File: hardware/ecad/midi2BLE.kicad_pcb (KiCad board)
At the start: 2 copper layers, 100 x 30 mm, 50 parts, among them J1 USB_C_Receptacle, J2 Conn_01x02, J4 Conn_01x07, J6 Conn_01x04, SW1 SW_Push, SW2 SW_Push, SW3 SW_SPDT, U1 BQ24079RGTT, U2 TPS62162DSG, U3 TLV61047DDC, U4 ESP32-S3-WROOM-1, U5 TPS2116DRL, U6 TS3USB30EDGSR

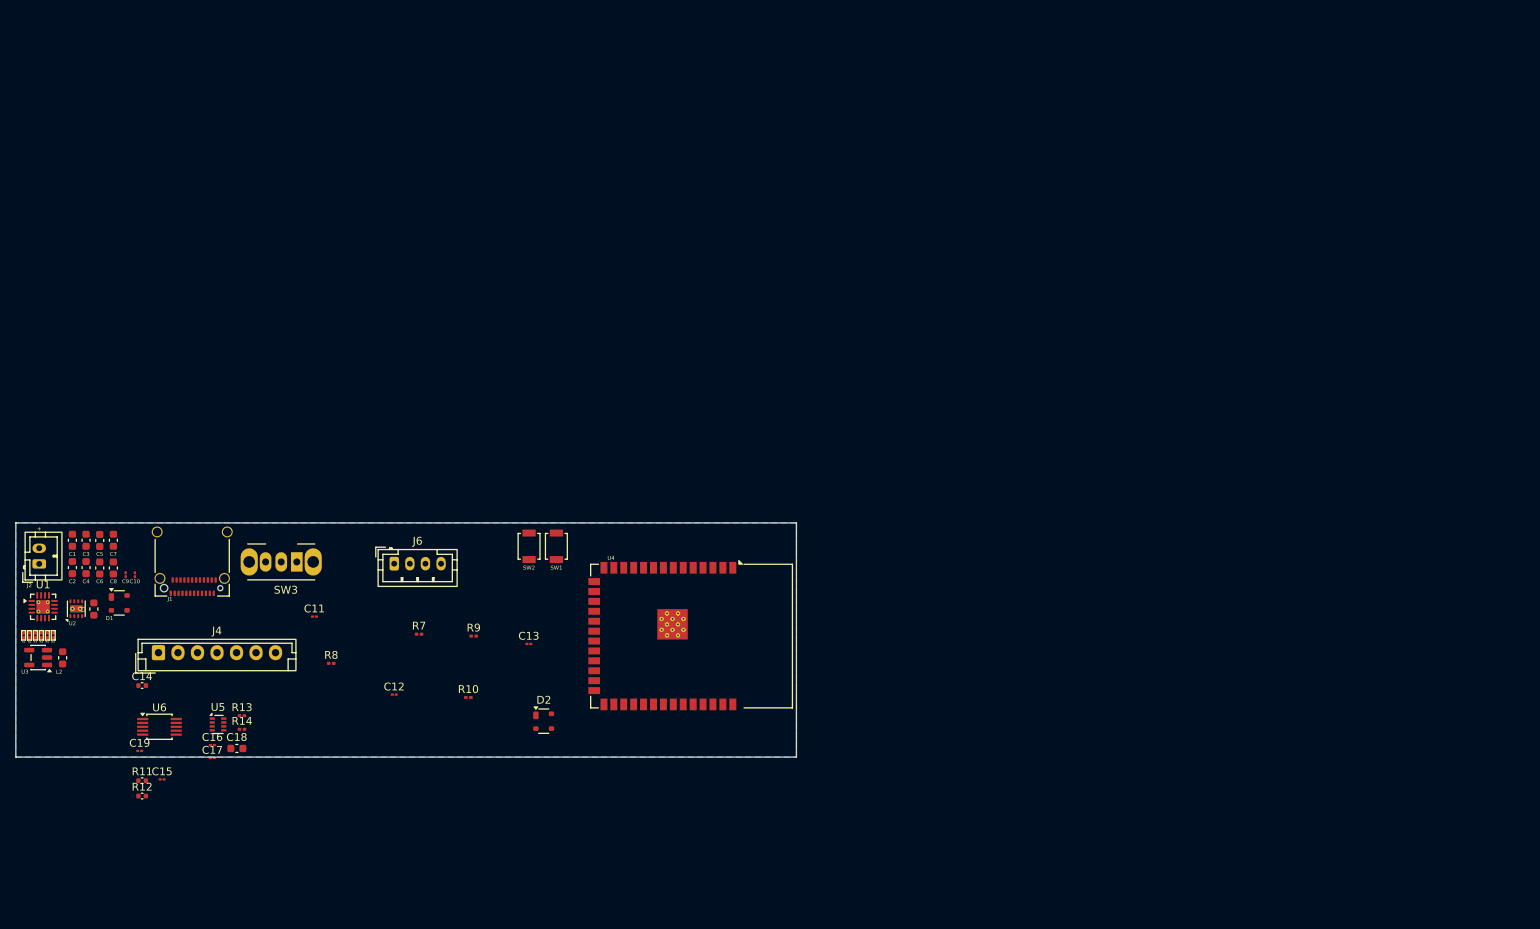
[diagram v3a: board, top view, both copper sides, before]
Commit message: Updated schematics and added printed pdf
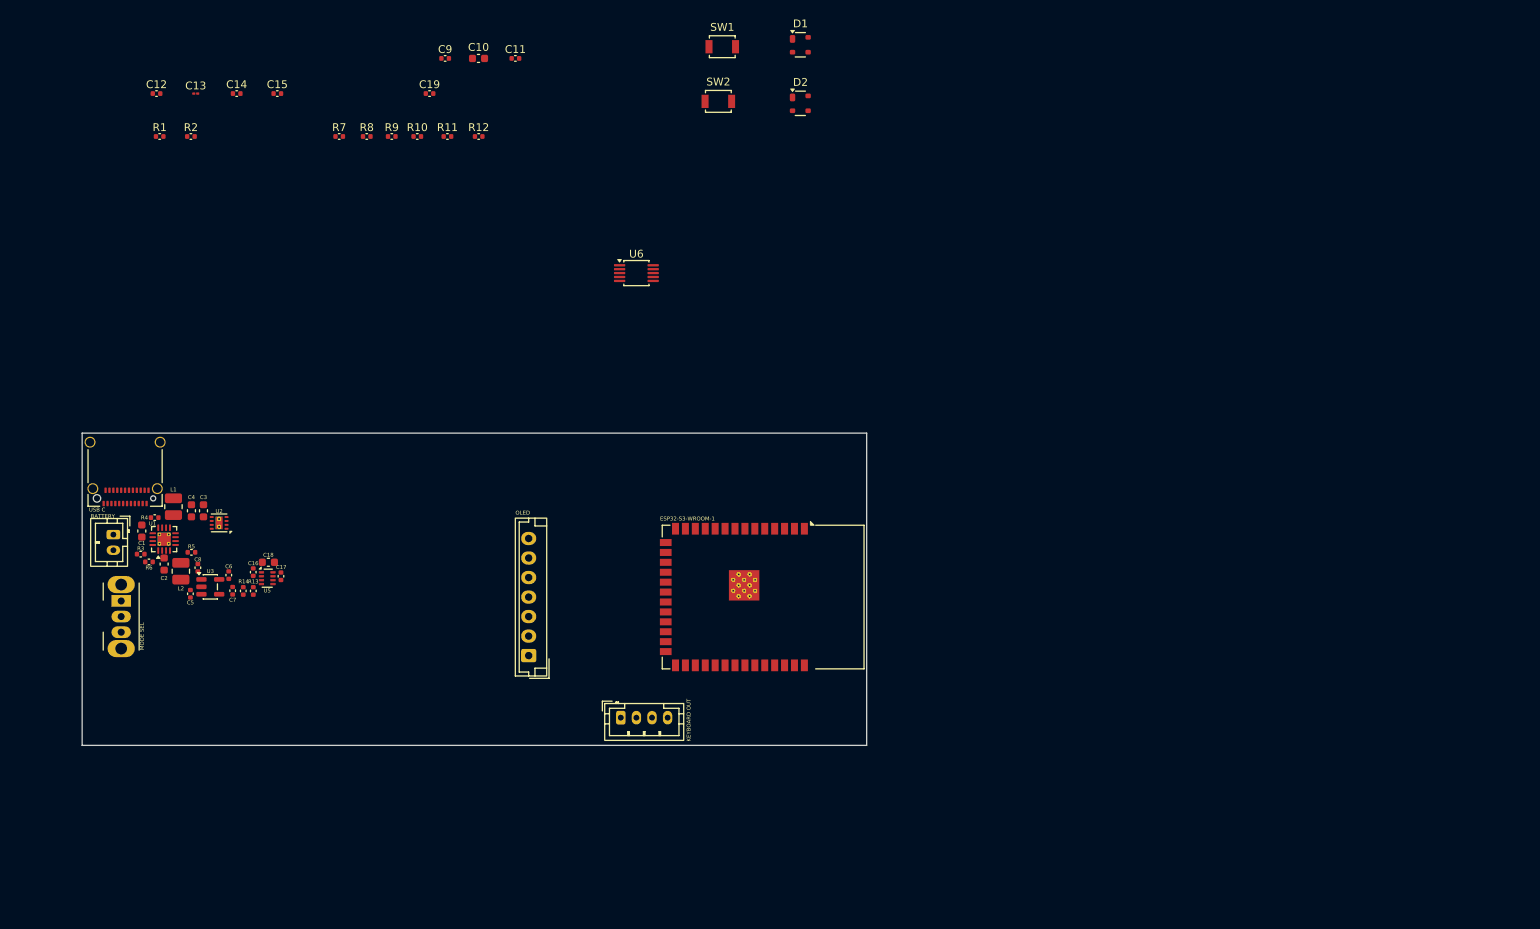
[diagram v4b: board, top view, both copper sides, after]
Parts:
- C10: footprint Capacitor_SMD:C_01005_0402Metric -> Capacitor_SMD:C_0603_1608Metric
- C11, C12, C15, C16, C17, C19, C9: footprint Capacitor_SMD:C_01005_0402Metric -> Capacitor_SMD:C_0402_1005Metric
- C5, C6, C7, C8: footprint Capacitor_SMD:C_0603_1608Metric -> Capacitor_SMD:C_0402_1005Metric
- L1, L2: footprint Inductor_SMD:L_0603_1608Metric -> Inductor_SMD:L_1008_2520Metric
- R1, R10, R13, R14, R2, R3, R4, R5, R6, R7, R8, R9: footprint Resistor_SMD:R_0201_0603Metric -> Capacitor_SMD:C_0402_1005Metric
- moved D1 112.8 mm to (191.0, 18.8)
- moved R12 94.9 mm to (149.8, 30.5)
- moved C19 92.0 mm to (143.5, 25.0)
- moved R11 91.3 mm to (145.8, 30.5)
- moved C15 89.1 mm to (124.0, 25.0)
- moved D2 85.7 mm to (191.0, 26.2)
- moved U6 84.3 mm to (170.0, 48.0)
- moved C12 82.8 mm to (108.5, 25.0)
- moved C13 82.4 mm to (113.5, 25.0)
- moved C10 79.5 mm to (149.8, 20.5), turned to 0 degrees
- moved C9 77.8 mm to (145.5, 20.5), turned to 0 degrees
- moved C14 76.8 mm to (118.8, 25.0)
- moved C11 76.0 mm to (154.5, 20.5)
- moved R10 72.2 mm to (141.9, 30.5)
- moved R8 67.7 mm to (135.5, 30.5)
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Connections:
- net /Power/U3 SW - L2 P1 renamed Net-(U3-SW)
- C4 pad 2: /Power/L2 P2 - C4 P1 -> BOOST_5V
- C5 pad 2: VBUS_IN -> BOOST_5V
- C8 pad 2: /Power/L2 P2 - C4 P1 -> BOOST_5V
- L2 pad 2: /Power/L2 P2 - C4 P1 -> BOOST_5V
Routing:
- removed copper zone on B.Cu, net /Power/U2 FB - C3 P1
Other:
- board size 100 x 30 mm -> 100.5 x 40 mm
- copper layers 2 -> 4
- board text added: "BATTERY"
- board text added: "ESP32-S3-WROOM-1"
- board text added: "KEYBOARD OUT"
- board text added: "MODE SEL"
- board text added: "OLED"
- board text added: "USB C"
- board text removed: "+"

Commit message: docs(hardware): update ecad README to reflect completed schematic and PCB — PCB IS DONE!!!
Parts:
- added TP1: TestPoint, TestPoint:TestPoint_THTPad_D1.0mm_Drill0.5mm, F.Cu at (160.8, 76.5)
- added TP2: TestPoint, TestPoint:TestPoint_THTPad_D1.0mm_Drill0.5mm, F.Cu at (163.5, 76.5)
- added TP3: TestPoint, TestPoint:TestPoint_THTPad_D1.0mm_Drill0.5mm, F.Cu at (160.0, 105.0)
- added TP4: TestPoint, TestPoint:TestPoint_THTPad_D1.0mm_Drill0.5mm, F.Cu at (157.8, 105.0)
- added TP5: TestPoint, TestPoint:TestPoint_THTPad_D1.0mm_Drill0.5mm, F.Cu at (158.0, 76.5)
- added TP6: TestPoint, TestPoint:TestPoint_THTPad_D1.0mm_Drill0.5mm, F.Cu at (155.5, 105.0)
- C13: footprint Capacitor_SMD:C_01005_0402Metric -> Capacitor_SMD:C_0402_1005Metric
- moved C12 96.1 mm to (165.0, 102.8)
- moved D1 94.8 mm to (112.2, 71.5), turned to -90 degrees
- moved D2 89.8 mm to (141.3, 101.1)
- moved SW2 80.8 mm to (164.5, 105.2)
- moved R8 76.5 mm to (160.8, 102.8)
- moved R10 71.9 mm to (109.8, 94.8), turned to 180 degrees
- moved C19 70.0 mm to (143.2, 95.0), turned to 180 degrees
- moved C13 68.3 mm to (125.2, 92.2), turned to 180 degrees
- moved C14 67.2 mm to (133.8, 90.5), turned to -90 degrees
- moved R9 61.2 mm to (125.2, 90.2)
- moved C10 60.5 mm to (166.0, 78.8)
- moved C9 59.4 mm to (166.0, 76.2)
- moved U6 57.2 mm to (141.3, 97.4)
- moved C15 55.5 mm to (154.8, 71.2), turned to 180 degrees
- moved SW1 54.6 mm to (163.0, 70.5)
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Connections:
- net USB_D+_ESP renamed USB_ESP+
- net USB_D+_UP renamed USB_UP+
- net USB_D-_ESP renamed USB_ESP-
- net USB_D-_UP renamed USB_UP-
- D2 pad 2: USB_D+_KBD -> USB_KBD+
- D2 pad 3: USB_D-_KBD -> USB_KBD-
- J6 pad 2: USB_D-_KBD -> USB_KBD+
- J6 pad 3: USB_D+_KBD -> USB_KBD-
- U6 pad 4: USB_D+_KBD -> USB_KBD+
- U6 pad 6: USB_D-_KBD -> USB_KBD-
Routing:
- net GND: track 0.00 -> 100.8 mm, vias 0 -> 16
- net BAT: track 0.00 -> 81.8 mm
- net MODE_SEL: track 0.00 -> 70.3 mm, vias 0 -> 5
- net VBUS_KBD: track 0.00 -> 61.8 mm, vias 0 -> 3
- net USB_UP-: track 0.00 -> 59.7 mm, vias 0 -> 2
- net USB_UP+: track 0.00 -> 59.0 mm, vias 0 -> 4
- net BOOST_5V: track 0.00 -> 56.4 mm
- net VBUS_IN: track 0.00 -> 52.7 mm, vias 0 -> 2
- net OLED_RES: track 0.00 -> 32.8 mm
- net /ESP32_S3/BOOT_BUTTON: track 0.00 -> 27.6 mm, vias 0 -> 2
- net SYS_3V3: track 0.00 -> 27.3 mm, vias 0 -> 5
- net OLED_MOSI: track 0.00 -> 22.7 mm
- net USB_ESP+: track 0.00 -> 22.3 mm, vias 0 -> 2
- net OLED_CLK: track 0.00 -> 22.0 mm
- net /Power/U2 FB - C3 P1: track 0.00 -> 21.5 mm, vias 0 -> 2
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- added copper zone on In1.Cu, net GND
- added copper zone on In2.Cu, net SYS_3V3
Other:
- board size 100.5 x 40 mm -> 75 x 40 mm
- board text added: "3V3"
- board text added: "BOOT"
- board text added: "EN"
- board text added: "GND"
- board text added: "IO"
- board text added: "KBD OUT"
- board text added: "RST"
- board text added: "RX"
- board text added: "TX"
- board text added: "UART"
- board text removed: "KEYBOARD OUT"

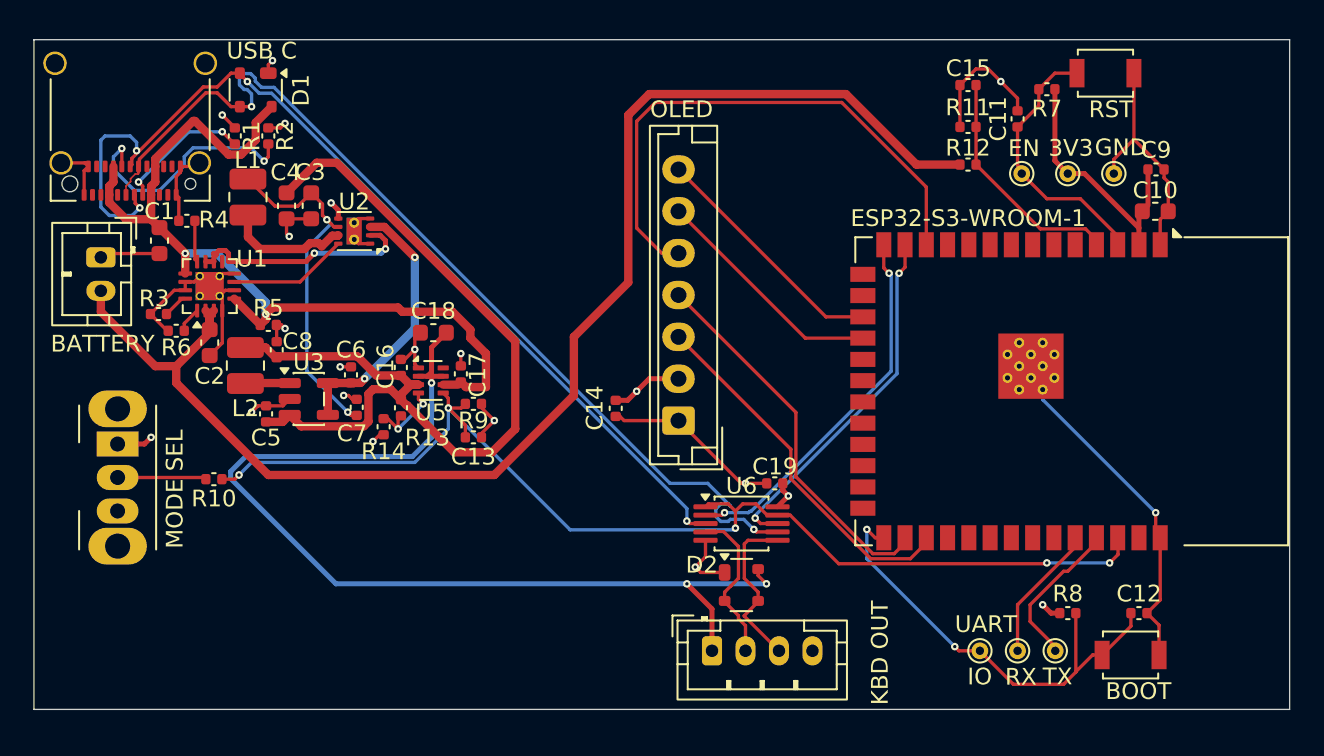
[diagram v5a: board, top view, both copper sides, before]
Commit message: Updated KiCad projectm and pcb, added in BOM
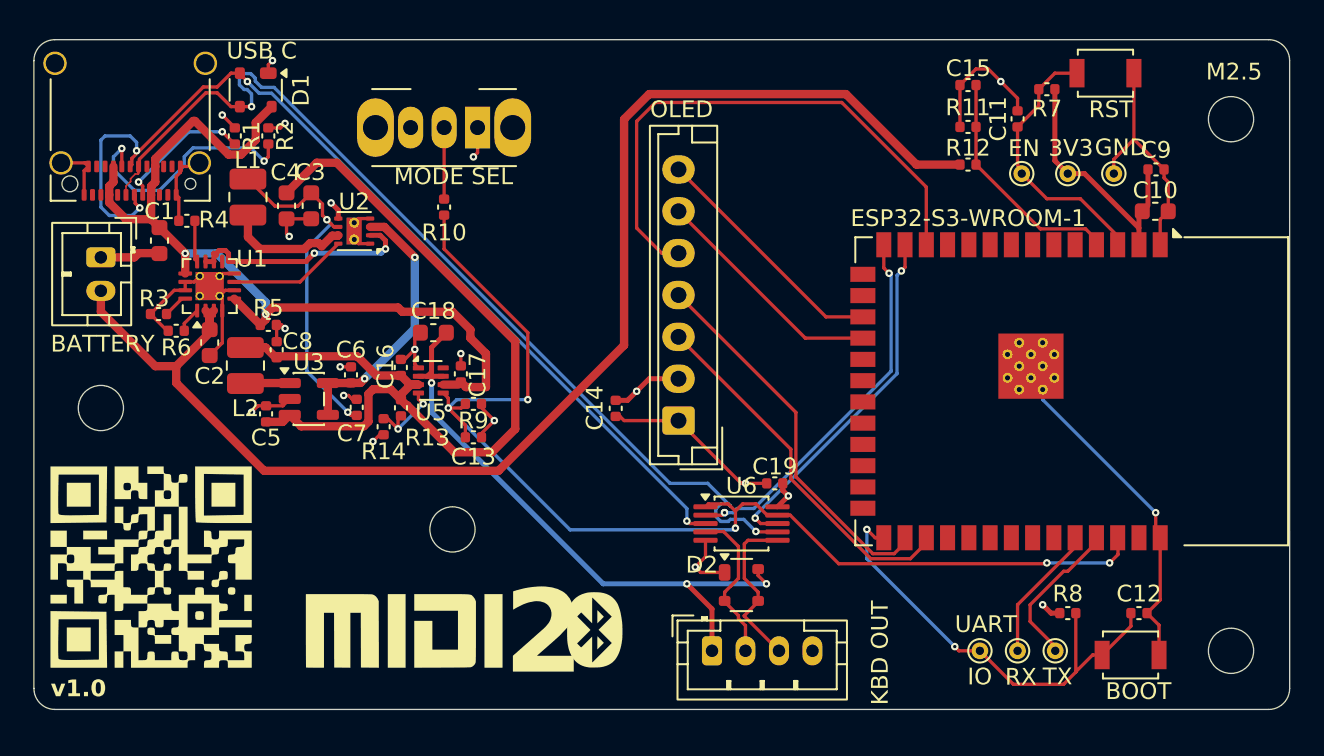
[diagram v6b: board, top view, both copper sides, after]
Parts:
- added G***: LOGO, LOGO, F.Cu at (106.0, 100.0)
- added G***: LOGO, LOGO, F.Cu at (132.5, 103.8)
- added G***: LOGO, LOGO, F.Cu at (121.2, 103.8)
- added G***: LOGO, LOGO, B.Cu at (132.2, 88.5)
- added REF**: MountingHole_2.7mm_M2.5, MountingHole:MountingHole_2.7mm_M2.5, F.Cu at (103.0, 90.5)
- added REF**: MountingHole_2.7mm_M2.5, MountingHole:MountingHole_2.7mm_M2.5, F.Cu at (170.5, 105.0)
- added REF**: MountingHole_2.7mm_M2.5, MountingHole:MountingHole_2.7mm_M2.5, F.Cu at (170.5, 73.2)
- added REF**: MountingHole_2.7mm_M2.5, MountingHole:MountingHole_2.7mm_M2.5, F.Cu at (124.0, 97.8)
- moved SW3 28.6 mm to (125.5, 73.8), turned to 180 degrees
- moved R10 21.3 mm to (123.5, 78.5), turned to 90 degrees
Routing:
- net VBUS_KBD: track 61.8 -> 36.7 mm
- net MODE_SEL: track 70.3 -> 72.3 mm
- net Net-(SW3-B): track 5.31 -> 4.27 mm
- net USB_ESP+: track 22.3 -> 23.3 mm
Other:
- outline, holes or cut-outs redrawn
- board text added: "2"
- board text added: "M2.5"
- board text added: "nikhilsudhir 2026"
- board text added: "v1.0"
